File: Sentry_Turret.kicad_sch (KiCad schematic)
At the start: 23 parts, among them J1 XT30_Y1, J11 24V_Agi2, J13 24V_Fly1, J15 24V_Fly3, J17 24V_Fly2, J19 24V_Fly4, J21 19V_Orin, J22 3.3V_Debug, J23 Conn_01x08, J3 XT30_P1, J5 XT30_P2, J7 XT30_Y2, J9 24V_Agi1

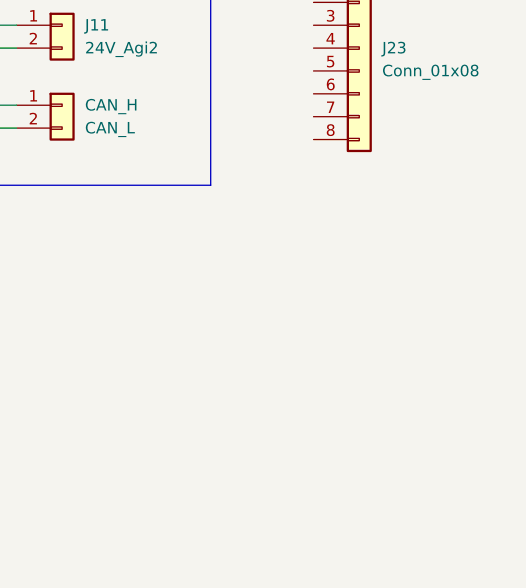
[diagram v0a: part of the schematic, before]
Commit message: Added connector and updated kicad lib
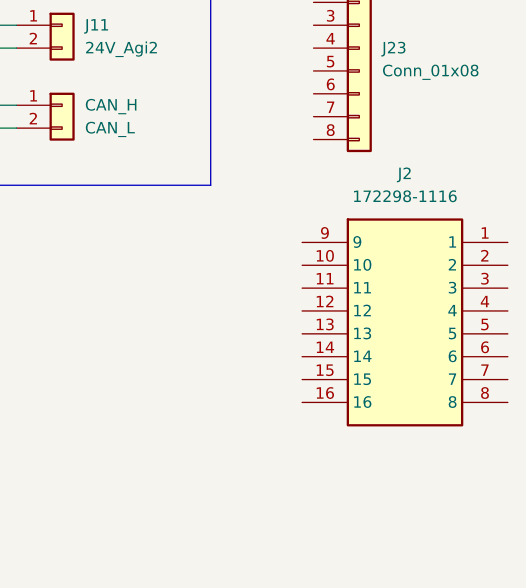
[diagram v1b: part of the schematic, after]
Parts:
- added J2: 172298-1116, 172298-YY16, symbol Robomaster_Library:172298-1116
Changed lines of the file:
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@@
+	)
+	(symbol
+		(lib_id "Robomaster_Library:172298-1116")
+		(at 187.96 58.42 0)
+		(unit 1)
+		(exclude_from_sim no)
+		(in_bom yes)
+		(on_board yes)
+		(dnp no)
+		(fields_autoplaced yes)
+		(property "Reference" "J2"
+			(at 199.39 50.8 0)
+			(effects
+				(font
+					(size 1.27 1.27)
+				)
+			)
+		)
+		(property "Value" "172298-1116"
+			(at 199.39 53.34 0)
+			(effects
+				(font
+					(size 1.27 1.27)
+				)
+			)
+		)
+		(property "Footprint" "172298-YY16"
+			(at 207.01 153.34 0)
+			(effects
+				(font
+					(size 1.27 1.27)
+				)
+				(justify left top)
+				(hide yes)
+			)
+		)
+		(property "Datasheet" "https://componentsearchengine.com/Datasheets/1/172298-1116.pdf"
+			(at 207.01 253.34 0)
+			(effects
+				(font
+					(size 1.27 1.27)
+				)
+				(justify left top)
+				(hide yes)
+			)
+		)
+		(property "Description" "Ultra-Fit Vertical Header, 3.50mm Pitch, Dual Row, 16 Circuits, with Kinked Pins, Glow-Wire Capable"
+			(at 187.96 58.42 0)
+			(effects
+				(font
+					(size 1.27 1.27)
+				)
+				(hide yes)
+			)
+		)
+		(property "Height" "14"
+			(at 207.01 453.34 0)
+			(effects
+				(font
+					(size 1.27 1.27)
+				)
+				(justify left top)
+				(hide yes)
+			)
+		)
+		(property "Mouser Part Number" "538-172298-1116"
+			(at 207.01 553.34 0)
+			(effects
+				(font
+					(size 1.27 1.27)
+				)
+				(justify left top)
+				(hide yes)
+			)
+		)
+		(property "Mouser Price/Stock" "https://www.mouser.com/Search/Refine.aspx?Keyword=538-172298-1116"
+			(at 207.01 653.34 0)
+			(effects
+				(font
+					(size 1.27 1.27)
+				)
+				(justify left top)
+				(hide yes)
+			)
+		)
+		(property "Manufacturer_Name" "Molex"
+			(at 207.01 753.34 0)
+			(effects
+				(font
+					(size 1.27 1.27)
+				)
+				(justify left top)
+				(hide yes)
+			)
+		)
+		(property "Manufacturer_Part_Number" "172298-1116"
+			(at 207.01 853.34 0)
+			(effects
+				(font
+					(size 1.27 1.27)
+				)
+				(justify left top)
+				(hide yes)
+			)
+		)
+		(pin "9"
+		)
+		(pin "6"
+		)
+		(pin "12"
+		)
+		(pin "1"
+		)
+		(pin "3"
+		)
+		(pin "5"
+		)
+		(pin "4"
+		)
+		(pin "10"
+		)
+		(pin "7"
+		)
+		(pin "8"
+		)
+		(pin "13"
+		)
+		(pin "14"
+		)
+		(pin "15"
+		)
+		(pin "16"
+		)
+		(pin "11"
+		)
+		(pin "2"
+		)
+		(instances
+			(project ""
+				(path "/1af64243-237e-4d0e-bea9-8a84ac1ea3bc"
+					(reference "J2")
+					(unit 1)
+				)
+			)
+		)
 	)
 	(symbol

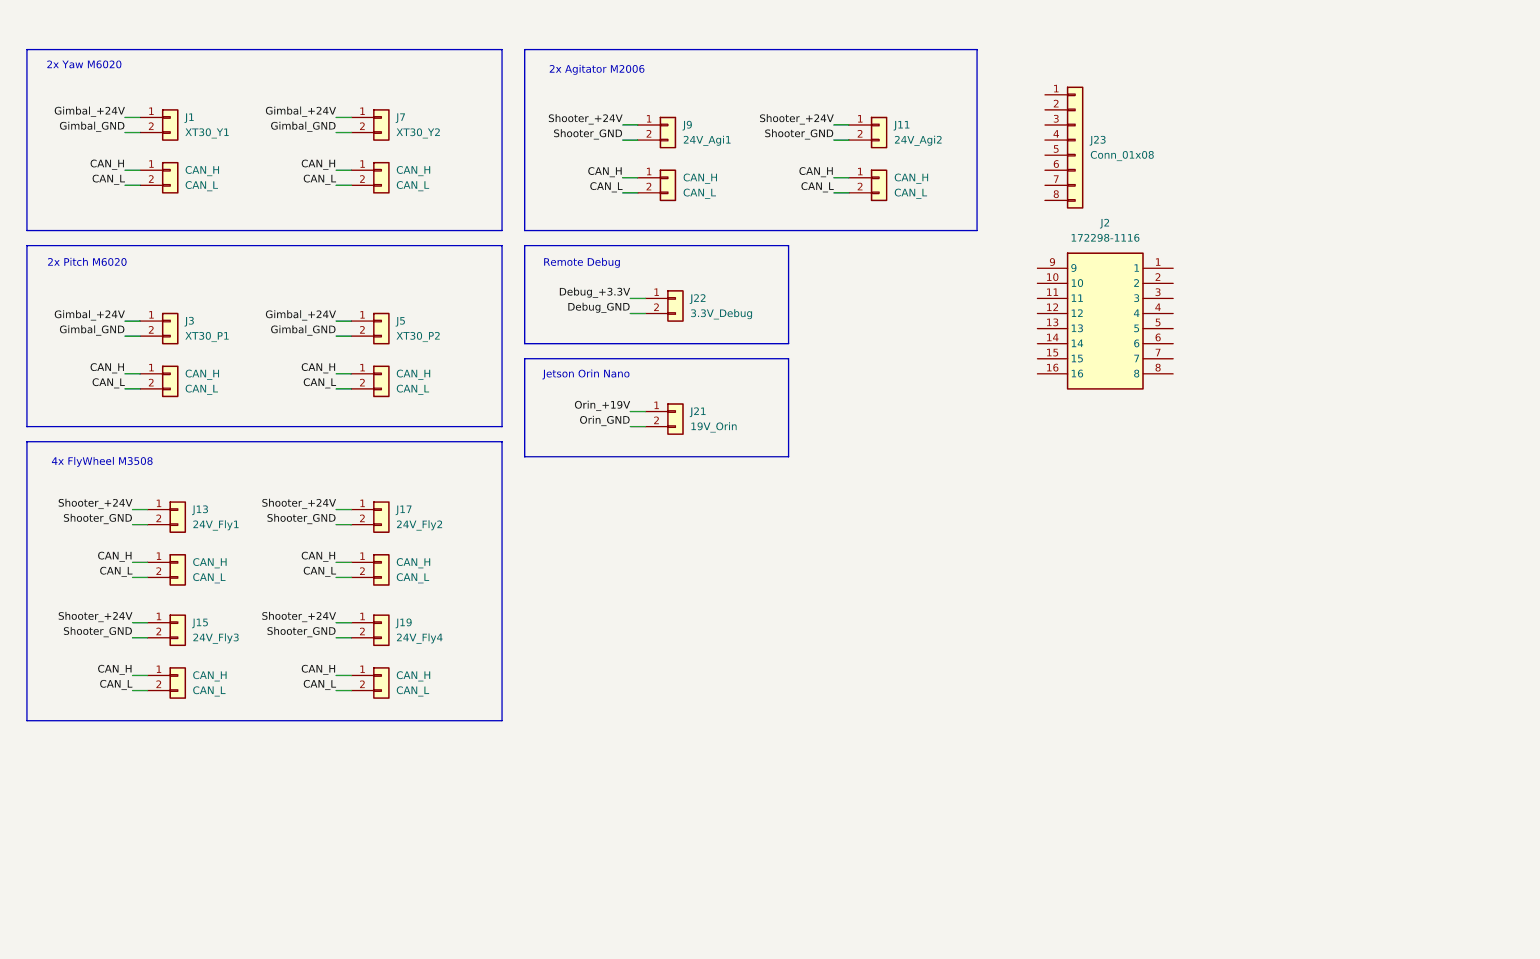
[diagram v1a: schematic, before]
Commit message: Added hierarchical labels
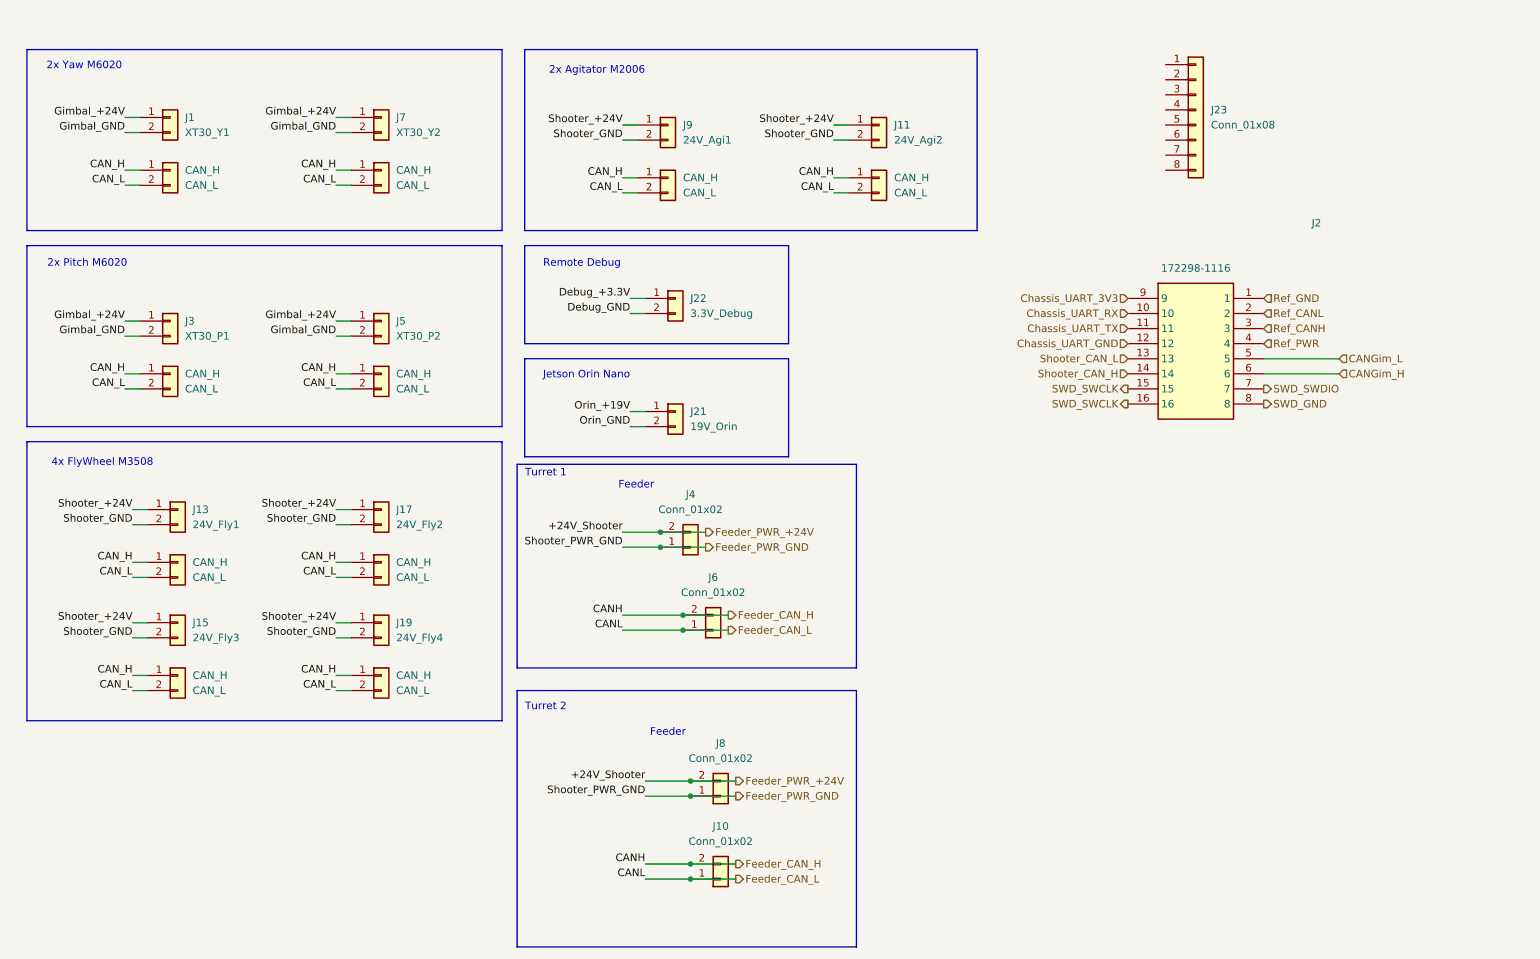
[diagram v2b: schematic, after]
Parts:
- added J10, J4, J6, J8: Conn_01x02, symbol Connector_Generic:Conn_01x02
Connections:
- net Ref_GND: now reaches J2.1
- net Chassis_UART_RX: now reaches J2.10
- net Chassis_UART_TX: now reaches J2.11
- net Chassis_UART_GND: now reaches J2.12
- net Shooter_CAN_L: now reaches J2.13
- net Shooter_CAN_H: now reaches J2.14
- net SWD_SWCLK: now reaches J2.15
- net SWD_SWCLK: now also J2.16
- net Ref_CANL: now reaches J2.2
- net Ref_CANH: now reaches J2.3
- net Ref_PWR: now reaches J2.4
- net CANGim_L: now reaches J2.5
- net CANGim_H: now reaches J2.6
- net SWD_SWDIO: now reaches J2.7
- net SWD_GND: now reaches J2.8
- net Chassis_UART_3V3: now reaches J2.9
- new net Feeder_CAN_H: J10.2 (Pin_2), J6.2 (Pin_2)
- new net Feeder_CAN_L: J10.1 (Pin_1), J6.1 (Pin_1)
- new net Feeder_PWR_+24V: J4.2 (Pin_2), J8.2 (Pin_2)
- new net Feeder_PWR_GND: J4.1 (Pin_1), J8.1 (Pin_1)
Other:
- note added: "Feeder"
- note added: "Turret 1"
- note added: "Turret 2"
- moved on the sheet: J2, J23

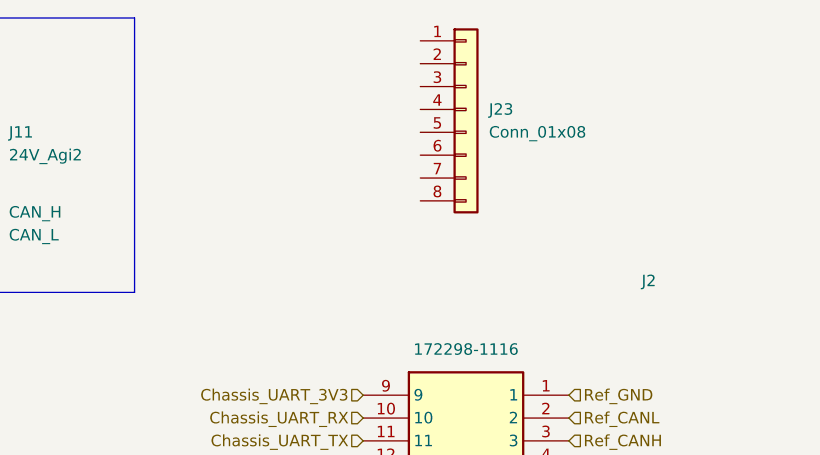
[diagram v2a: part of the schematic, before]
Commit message: add labels to sentry turret connector
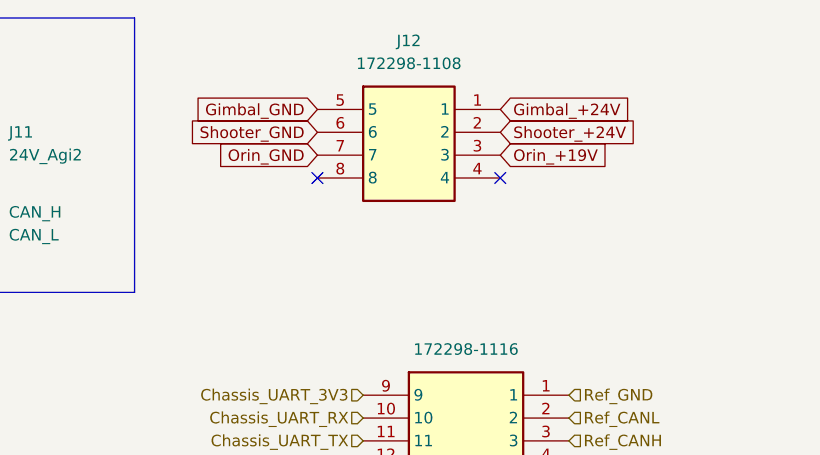
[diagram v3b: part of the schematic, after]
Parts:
- removed J23: Conn_01x08, symbol Connector_Generic:Conn_01x08
- added J12: 172298-1108, 172298-YY08, symbol Robomaster:172298-1108
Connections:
- net Gimbal_+24V: now also J12.1
- net Gimbal_GND: now also J12.5
- net Orin_+19V: now also J12.3
- net Orin_GND: now also J12.7
- net Shooter_+24V: now also J12.2
- net Shooter_GND: now also J12.6
- no-connect marks 0 -> 2
